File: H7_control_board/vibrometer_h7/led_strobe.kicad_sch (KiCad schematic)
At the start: 26 parts, among them Q1001 NPN

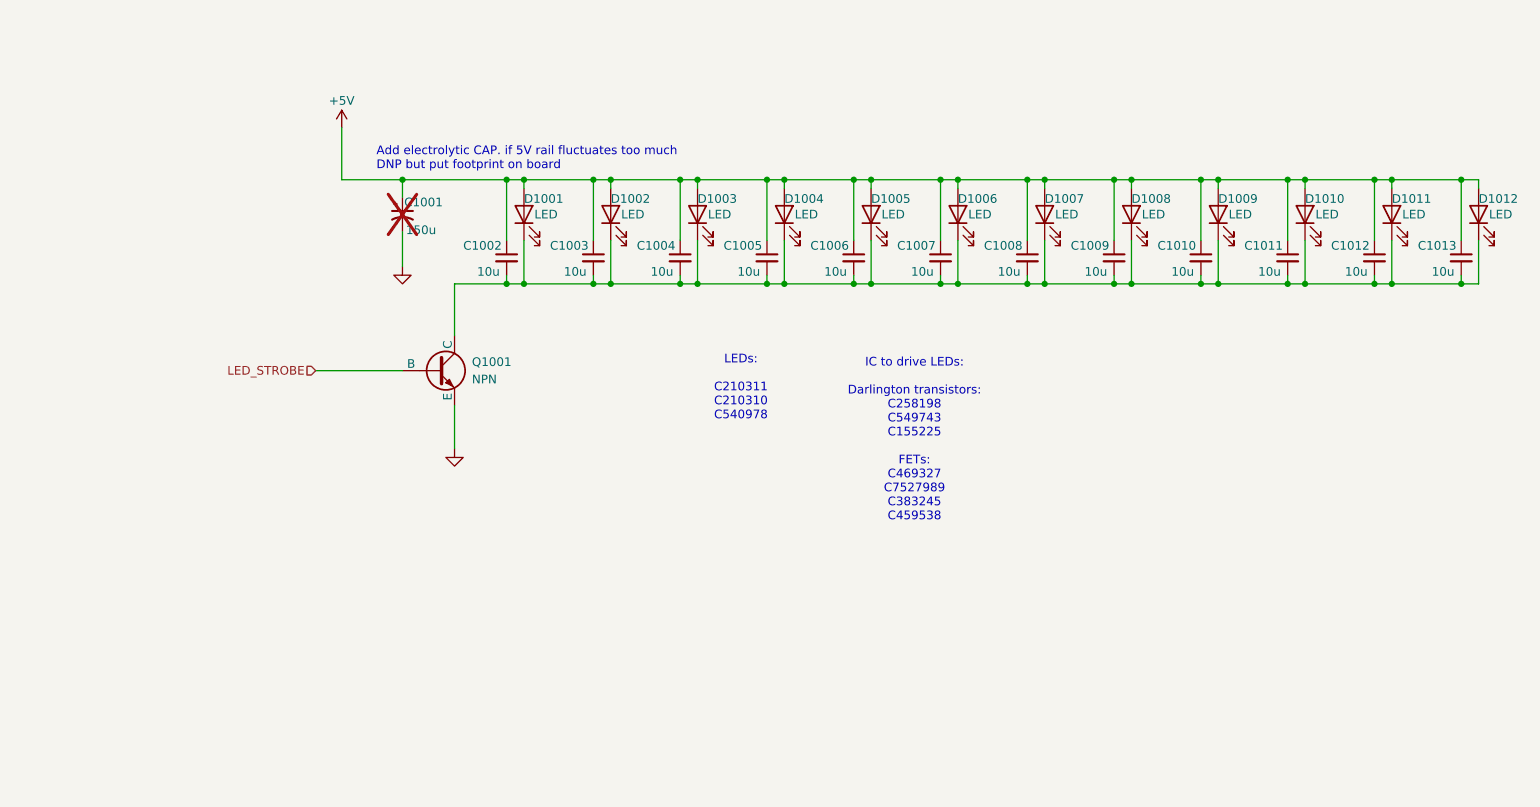
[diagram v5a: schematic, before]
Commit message: more decoupling caps, added level shifter to ws2812 led signal line
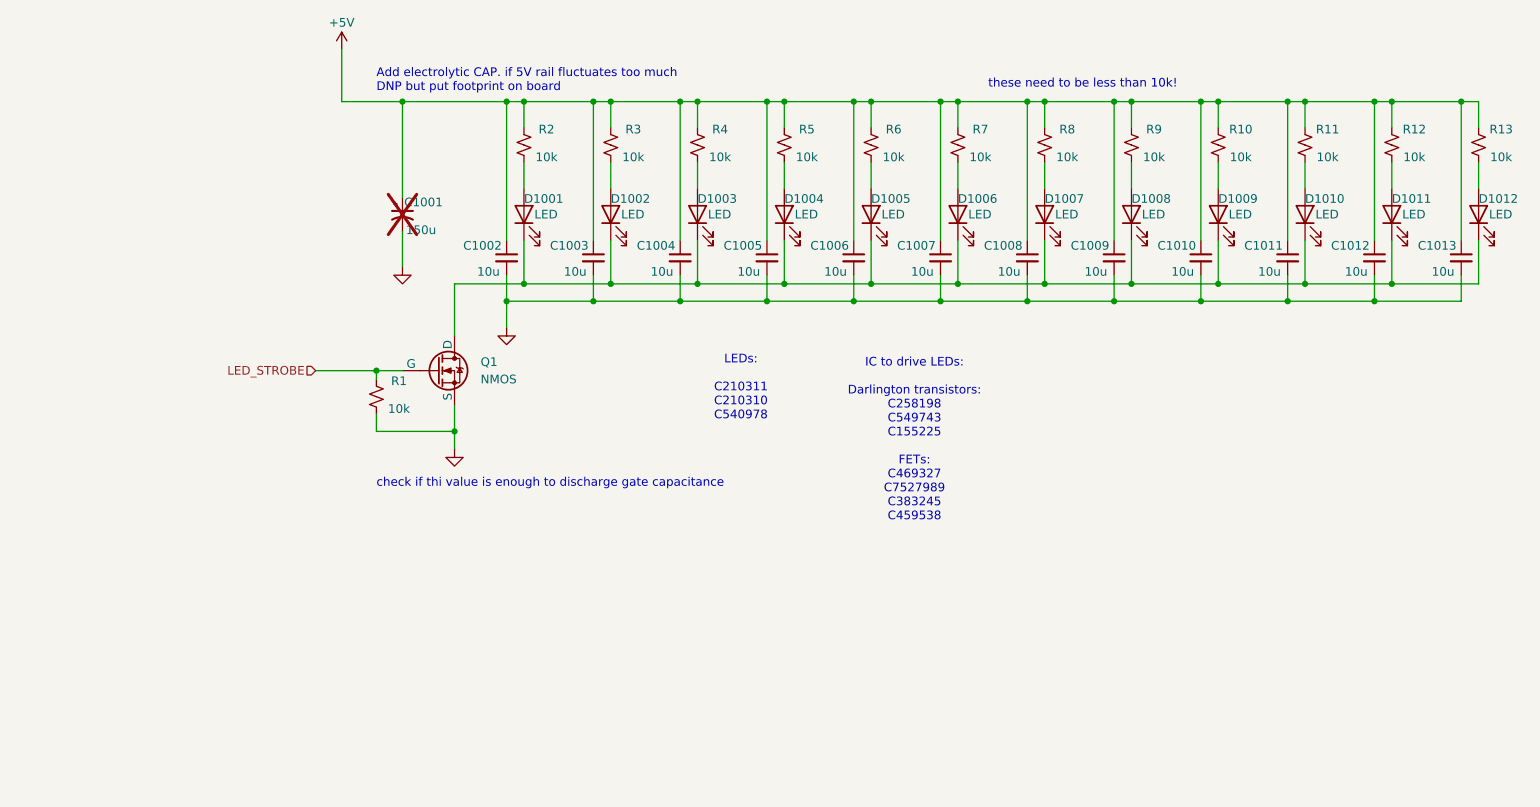
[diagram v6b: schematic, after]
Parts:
- removed Q1001: NPN, symbol Simulation_SPICE:NPN
- added Q1: NMOS, symbol Simulation_SPICE:NMOS
- added R1, R10, R11, R12, R13, R2, R3, R4, R5, R6, R7, R8, R9: 10k, symbol Device:R_Small_US
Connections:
- net +5V: now also R10.2, R11.2, R12.2, R13.2, R2.2, R3.2, R4.2, R5.2, R6.2, R7.2, R8.2, R9.2; no longer D1001.2 (A), D1002.2 (A), D1003.2 (A), D1004.2 (A), D1005.2 (A), D1006.2 (A), D1007.2 (A), D1008.2 (A), D1009.2 (A), D1010.2 (A), D1011.2 (A), D1012.2 (A)
- net GND: now also C1002.2, C1003.2, C1004.2, C1005.2, C1006.2, C1007.2, C1008.2, C1009.2, C1010.2, C1011.2, C1012.2, C1013.2, Q1.3 (S), R1.1
- net LED_STROBE: now also Q1.2 (G), R1.2
- net at D1001.1 (K), D1002.1 (K), D1003.1 (K)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: now also Q1.1 (D); no longer C1002.2, C1003.2, C1004.2, C1005.2, C1006.2, C1007.2, C1008.2, C1009.2, C1010.2, C1011.2, C1012.2, C1013.2
- new net: D1007.2 (A), R8.1
- new net: D1006.2 (A), R7.1
- new net: D1005.2 (A), R6.1
- new net: D1010.2 (A), R11.1
- new net: D1011.2 (A), R12.1
- new net: D1003.2 (A), R4.1
- new net: D1001.2 (A), R2.1
- new net: D1008.2 (A), R9.1
- new net: D1002.2 (A), R3.1
- new net: D1012.2 (A), R13.1
- new net: D1009.2 (A), R10.1
- new net: D1004.2 (A), R5.1
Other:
- note added: "check if thi value is enough to discharge gate capacitance"
- note added: "these need to be less than 10k!"

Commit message: selected strobe LEDs, schematic cleanup
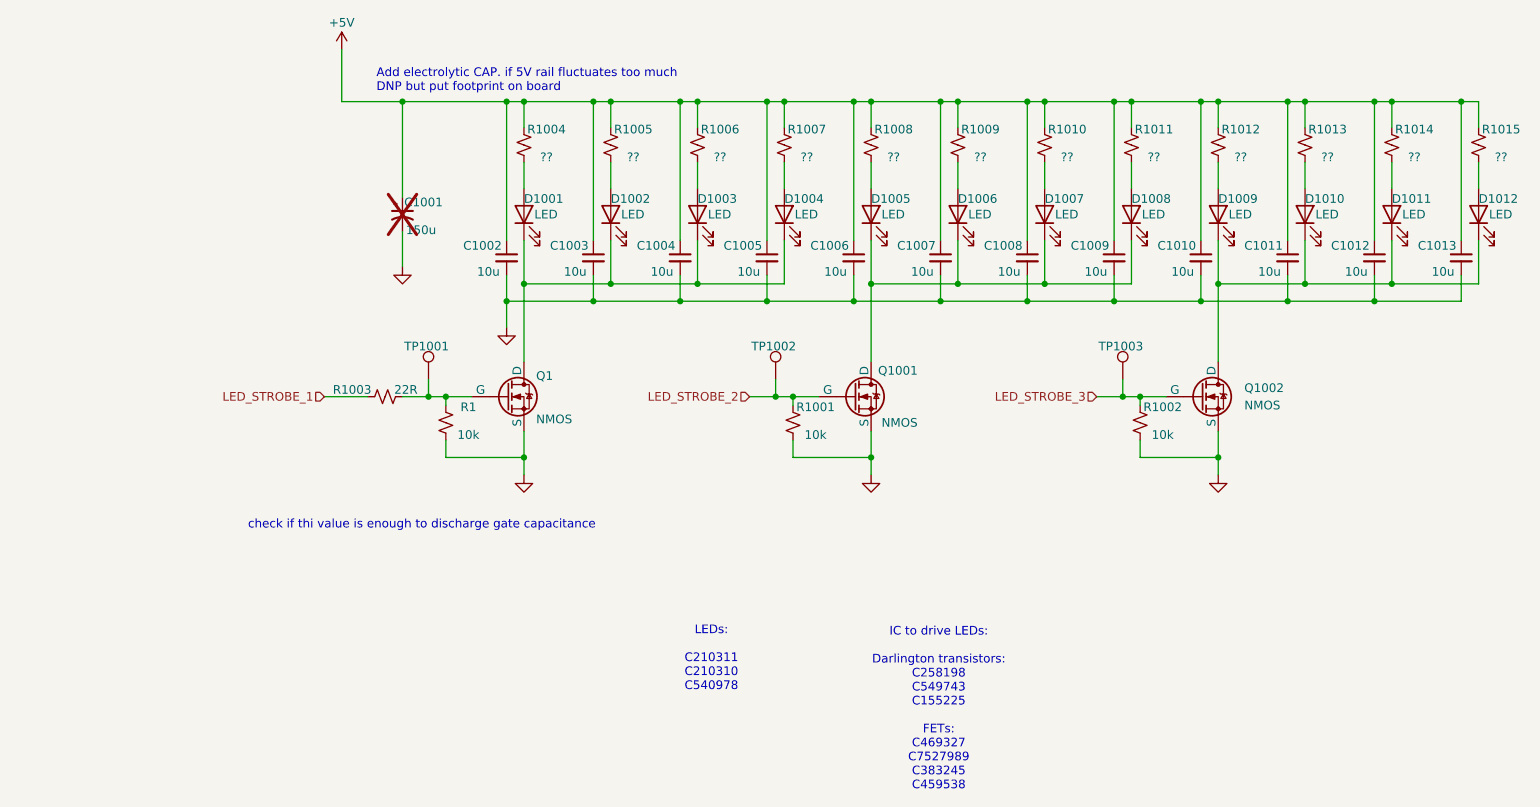
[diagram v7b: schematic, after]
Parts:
- removed R10, R11, R12, R13, R2, R3, R4, R5, R6, R7, R8, R9: 10k, symbol Device:R_Small_US
- added Q1001, Q1002: NMOS, symbol Simulation_SPICE:NMOS
- added R1001, R1002: 10k, symbol Device:R_Small_US
- added R1003: 22R, symbol Device:R_Small_US
- added R1004, R1005, R1006, R1007, R1008, R1009, R1010, R1011, R1012, R1013, R1014, R1015: ??, symbol Device:R_Small_US
- added TP1001, TP1002, TP1003: TestPoint, TestPoint:TestPoint_Pad_D1.5mm, symbol Connector:TestPoint
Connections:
- net +5V: now also R1004.2, R1005.2, R1006.2, R1007.2, R1008.2, R1009.2, R1010.2, R1011.2, R1012.2, R1013.2, R1014.2, R1015.2
- net GND: now also Q1001.3 (S), Q1002.3 (S), R1001.1, R1002.1
- net at D1007.2 (A): now also R1010.1
- net at D1006.2 (A): now also R1009.1
- net at D1005.2 (A): now also R1008.1
- net at D1010.2 (A): now also R1013.1
- net at D1011.2 (A): now also R1014.1
- net at D1003.2 (A): now also R1006.1
- net at D1001.2 (A): now also R1004.1
- net at D1008.2 (A): now also R1011.1
- net at D1002.2 (A): now also R1005.1
- net at D1012.2 (A): now also R1015.1
- net at D1009.2 (A): now also R1012.1
- net at D1004.2 (A): now also R1007.1
- net LED_STROBE: no longer names the net of Q1.2 (G), R1.2
- net LED_STROBE: now also R1003.1, TP1001.1
- new net: D1005.1 (K), D1006.1 (K), D1007.1 (K), D1008.1 (K), Q1001.1 (D)
- new net: D1001.1 (K), D1002.1 (K), D1003.1 (K), D1004.1 (K), Q1.1 (D)
- new net: D1009.1 (K), D1010.1 (K), D1011.1 (K), D1012.1 (K), Q1002.1 (D)
- new net LED_STROBE_1: R1003.2
- new net LED_STROBE_2: Q1001.2 (G), R1001.2, TP1002.1
- new net LED_STROBE_3: Q1002.2 (G), R1002.2, TP1003.1
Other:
- note removed: "these need to be less than 10k!"
- moved on the sheet: Q1, R1

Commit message: first pass at board routing
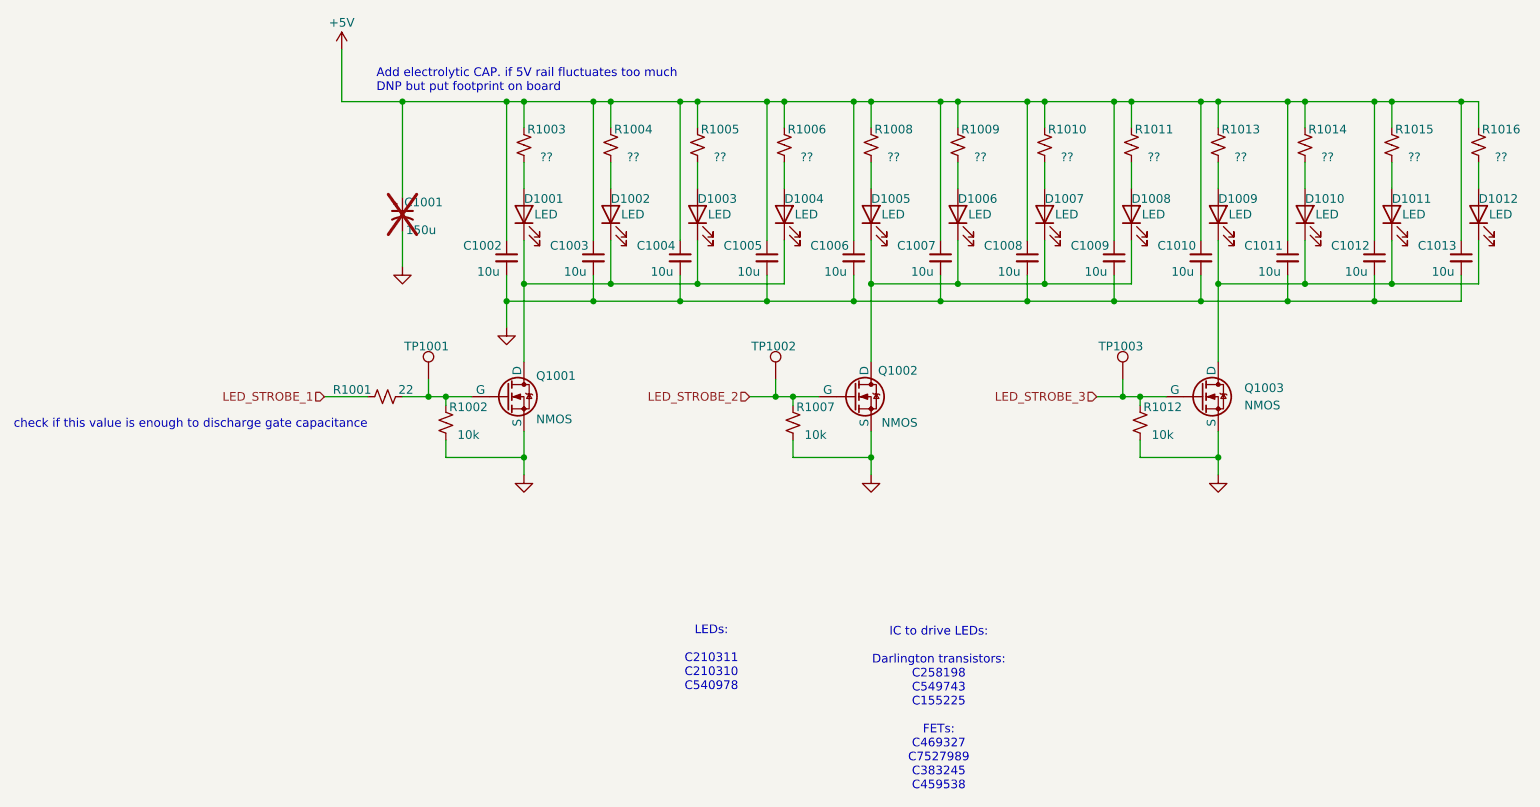
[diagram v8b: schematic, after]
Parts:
- C1001: footprint (none) -> Capacitor_SMD:CP_Elec_6.3x7.7; LCSC (none) -> C3032176
- C1002, C1003, C1004, C1005, C1006, C1007, C1008, C1009, C1010, C1011, C1012, C1013: footprint (none) -> Capacitor_SMD:C_0805_2012Metric; LCSC (none) -> C15850
- D1001, D1002, D1003, D1004, D1005, D1006, D1007, D1008, D1009, D1010, D1011, D1012: footprint (none) -> footprints:LED-SMD_L4.0-W1.50_HL-A-4014H421W-S1-HR3-DM-HL; LCSC (none) -> C540978
- R1001: renamed from R1003; value 22R -> 22; footprint (none) -> Resistor_SMD:R_0402_1005Metric; LCSC (none) -> C25092
- R1002: renamed from R1; footprint (none) -> Resistor_SMD:R_0603_1608Metric; LCSC (none) -> C25744
- R1003: renamed from R1004; footprint (none) -> Resistor_SMD:R_0805_2012Metric
- R1004: renamed from R1005; footprint (none) -> Resistor_SMD:R_0805_2012Metric
- R1005: renamed from R1006; footprint (none) -> Resistor_SMD:R_0805_2012Metric
- R1006: renamed from R1007; footprint (none) -> Resistor_SMD:R_0805_2012Metric
- R1007: renamed from R1001; footprint (none) -> Resistor_SMD:R_0603_1608Metric; LCSC (none) -> C25744
- R1008, R1009, R1010, R1011: footprint (none) -> Resistor_SMD:R_0805_2012Metric
- R1012: renamed from R1002; footprint (none) -> Resistor_SMD:R_0603_1608Metric; LCSC (none) -> C25744
- R1013: renamed from R1012; footprint (none) -> Resistor_SMD:R_0805_2012Metric
- R1014: renamed from R1013; footprint (none) -> Resistor_SMD:R_0805_2012Metric
- R1015: renamed from R1014; footprint (none) -> Resistor_SMD:R_0805_2012Metric
- R1016: renamed from R1015; footprint (none) -> Resistor_SMD:R_0805_2012Metric
- TP1001, TP1002, TP1003: footprint TestPoint:TestPoint_Pad_D1.5mm -> TestPoint:TestPoint_Pad_D1.0mm
- renumbered Q1 to Q1001, Q1001 to Q1002, Q1002 to Q1003
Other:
- note added: "check if this value is enough to discharge gate capacitance"
- note removed: "check if thi value is enough to discharge gate capacitance"
